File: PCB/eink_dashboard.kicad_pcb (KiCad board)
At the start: 2 copper layers, 60 parts, among them J1 USB_B_Micro, J2 Conn_01x05, Q1 IRLML6402, Q2 IRLML6402, Q3 IRLML6402, Q4 IRLML6402, U1 LM358, U10 CD4094, U11 CD4094, U2 MCP73831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

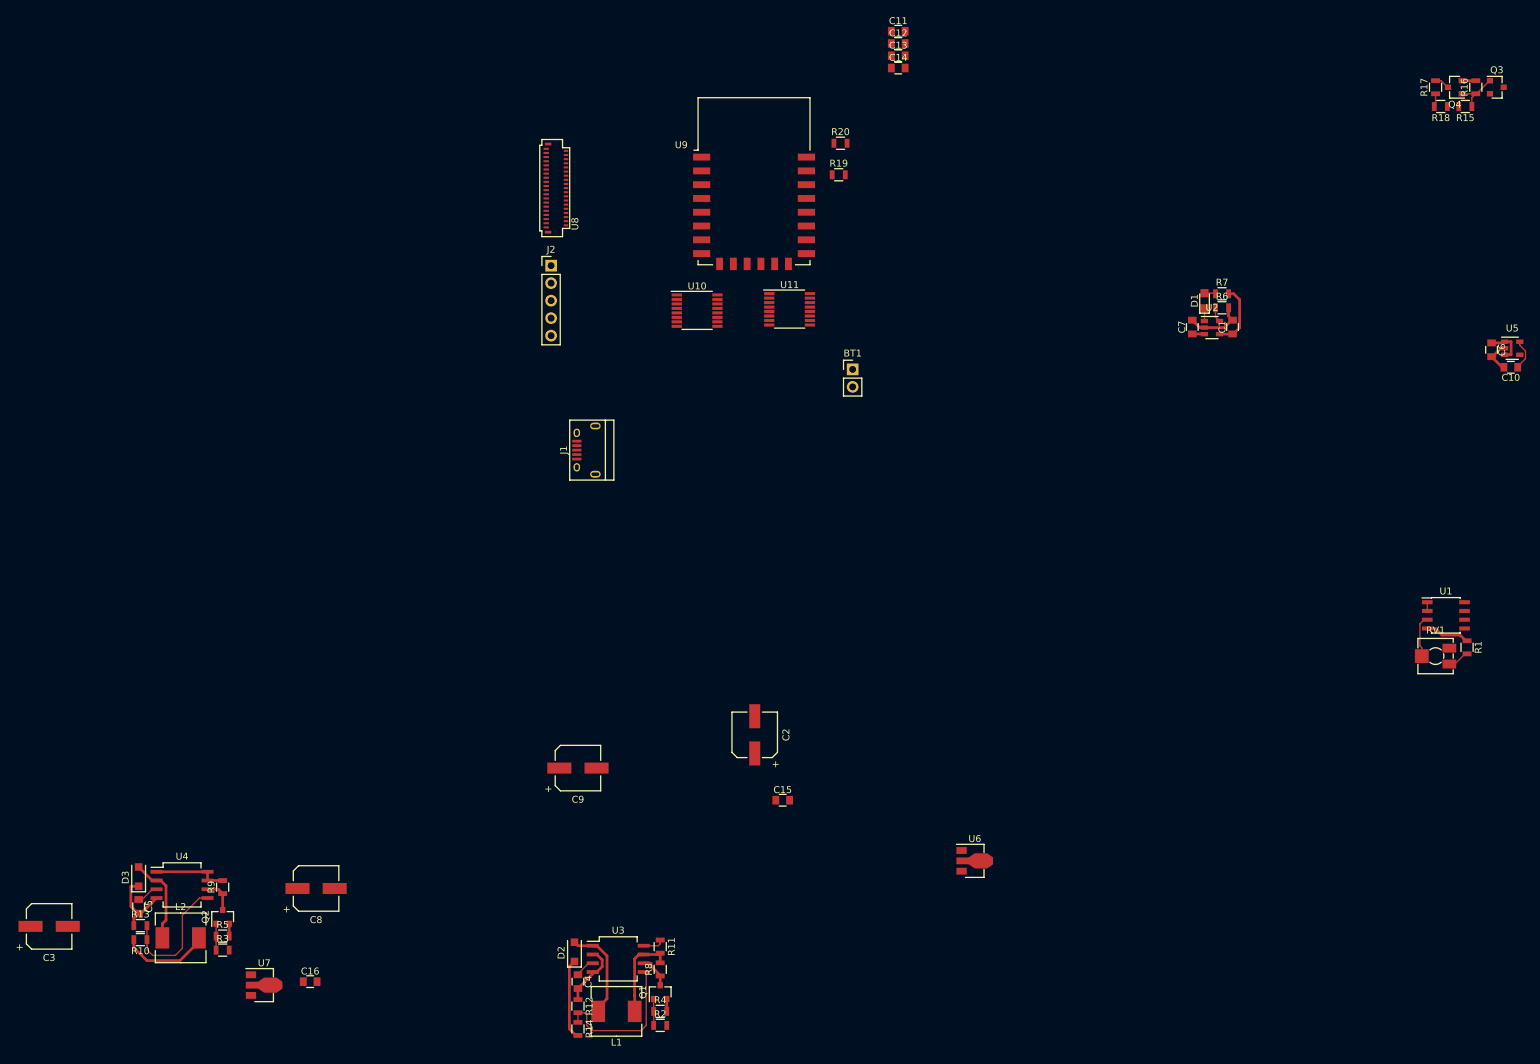
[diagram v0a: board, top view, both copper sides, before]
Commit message: PCB mostly routed
Final board layout defined
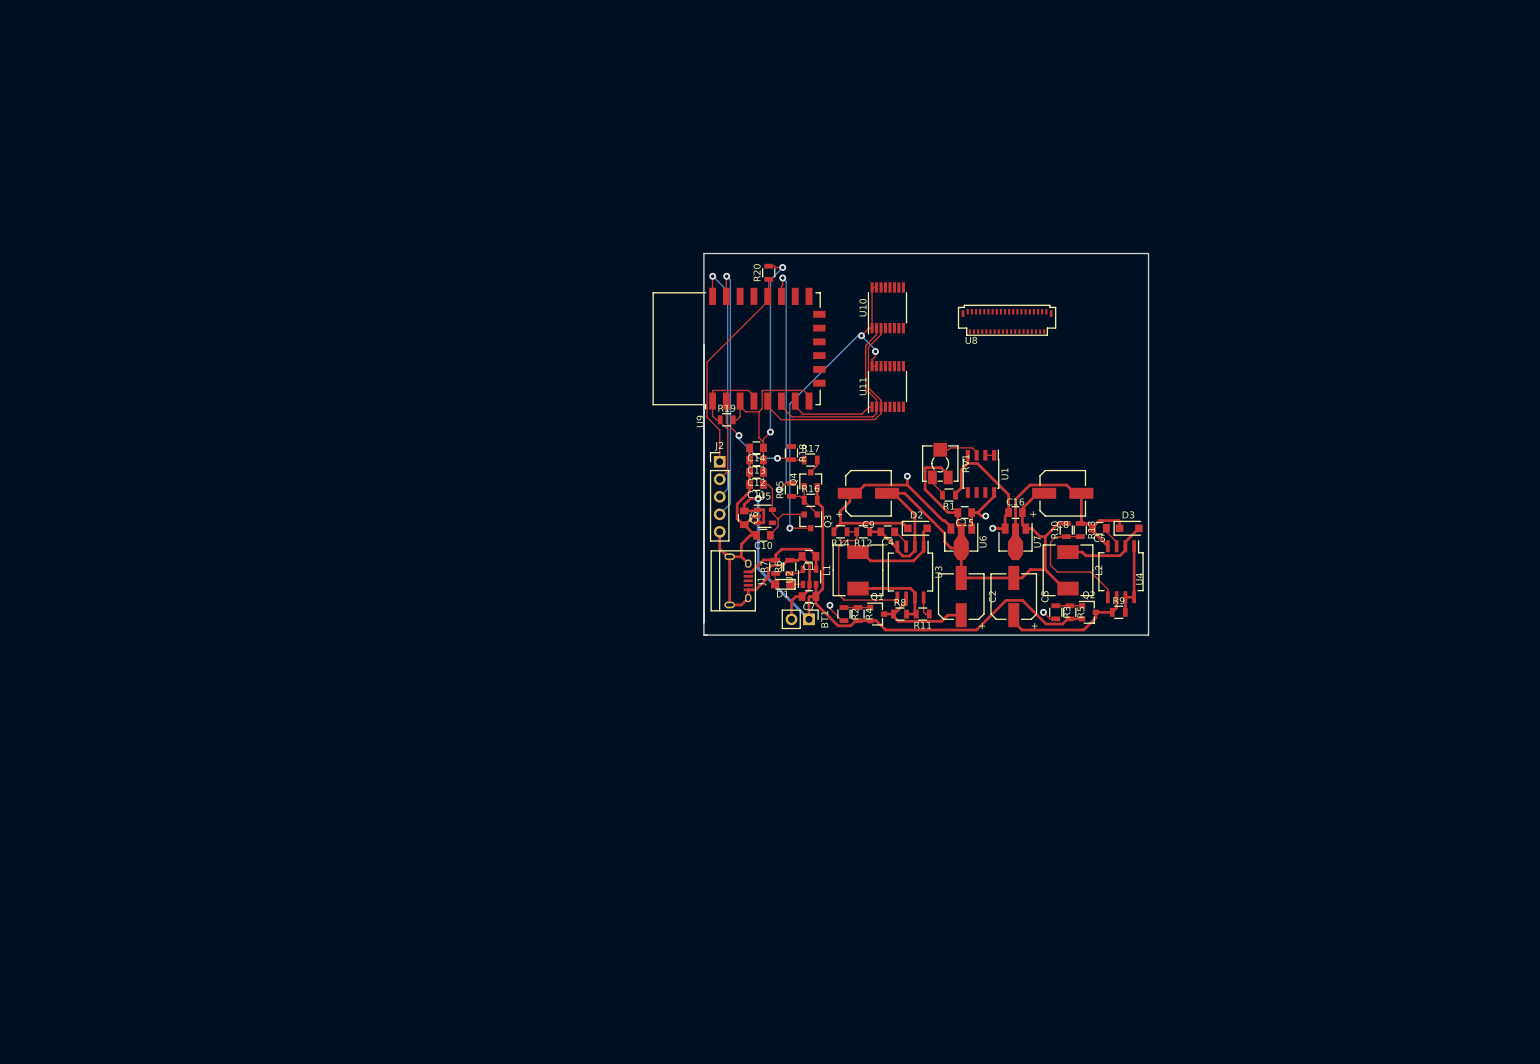
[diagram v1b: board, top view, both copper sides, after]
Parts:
- moved D3 152.4 mm to (180.8, 106.7), turned to 0 degrees
- moved C5 149.9 mm to (176.5, 106.7), turned to 180 degrees
- moved R13 148.0 mm to (173.7, 106.9), turned to 270 degrees
- moved C3 147.9 mm to (164.1, 116.6), turned to 90 degrees
- moved R10 146.9 mm to (171.7, 106.9), turned to 90 degrees
- moved U4 143.6 mm to (179.6, 113.0), turned to 270 degrees
- moved L2 139.4 mm to (172.0, 112.8), turned to 270 degrees
- moved R9 136.0 mm to (179.3, 118.9), turned to 0 degrees
- moved Q2 133.3 mm to (175.0, 118.9), turned to 0 degrees
- moved R5 131.6 mm to (172.2, 118.9), turned to 270 degrees
- moved R3 130.5 mm to (170.2, 118.9), turned to 270 degrees
- moved U7 127.2 mm to (164.3, 108.2), turned to 270 degrees
- moved C16 122.9 mm to (164.3, 104.4)
- moved C8 122.6 mm to (171.2, 101.6)
- moved Q3 117.8 mm to (134.6, 105.7), turned to 270 degrees
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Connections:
- U9 pad 6: STR -> D
- U9 pad 7: D -> STR
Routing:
- net GND: track 35.4 -> 156.4 mm
- net +BATT: track 13.1 -> 97.8 mm, vias 0 -> 1
- net +3V3: track 4.60 -> 71.1 mm, vias 0 -> 2
- net EINK_VDD: track 0.00 -> 50.2 mm, vias 0 -> 3
- net Net-(J2-Pad4): track 0.00 -> 38.3 mm, vias 0 -> 1
- net Net-(J2-Pad3): track 0.00 -> 36.3 mm, vias 0 -> 1
- net EINK_EN: track 0.00 -> 36.3 mm, vias 0 -> 2
- net CLK: track 0.00 -> 32.3 mm
- net Net-(J2-Pad1): track 0.00 -> 31.0 mm
- net D: track 0.00 -> 29.1 mm
- net -20V: track 11.1 -> 35.5 mm
- net +22V: track 11.7 -> 35.8 mm, vias 0 -> 1
- net ~RST: track 0.00 -> 21.7 mm
- net Net-(R17-Pad1): track 1.92 -> 17.0 mm, vias 0 -> 2
- net Net-(C3-Pad1): track 4.82 -> 19.7 mm
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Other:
- board outline added: 64.5 x 55.4 mm

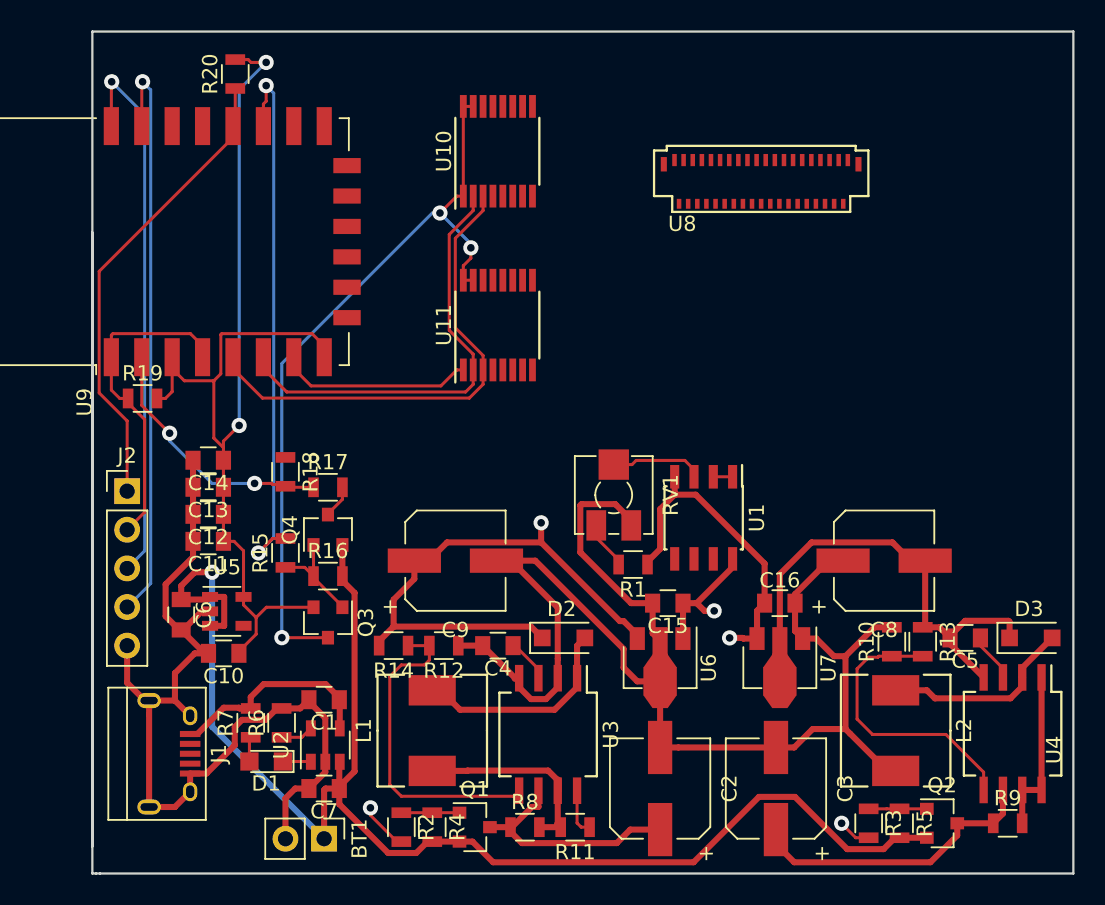
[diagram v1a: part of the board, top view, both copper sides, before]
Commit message: Finished routing board
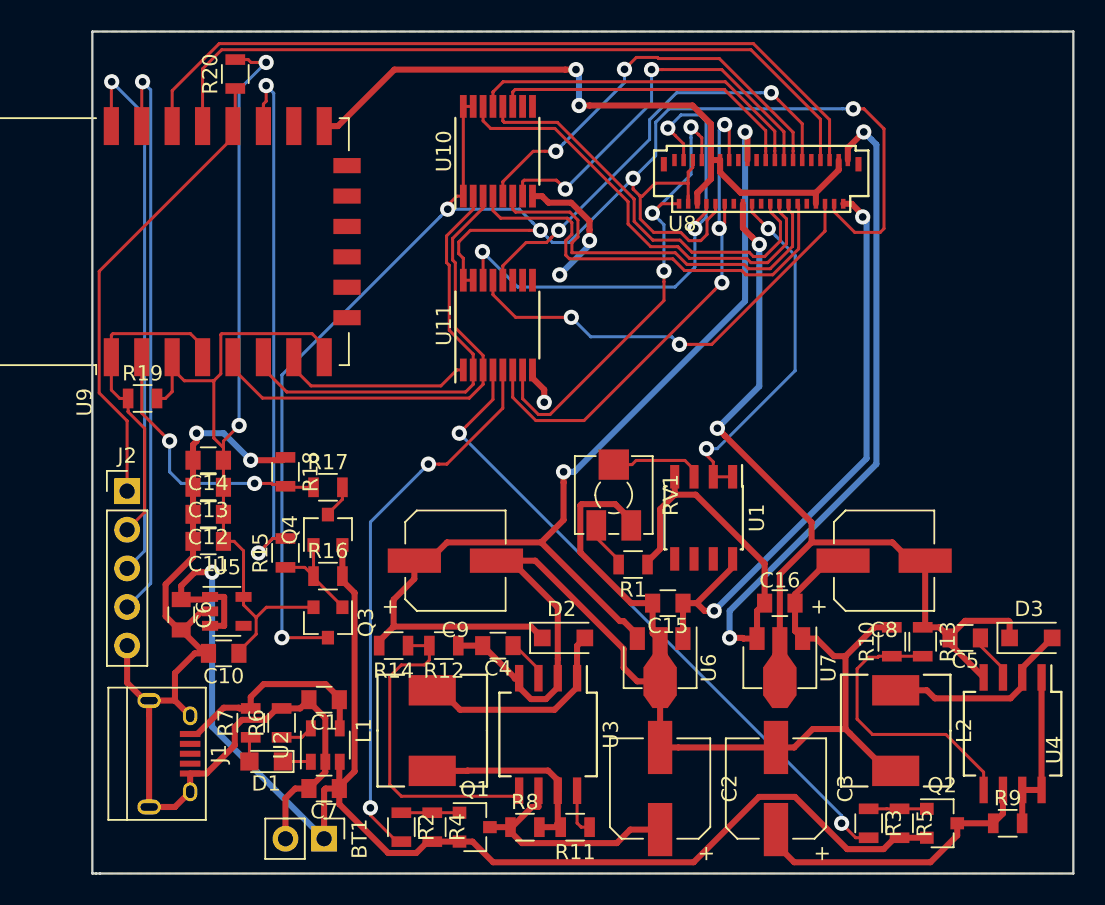
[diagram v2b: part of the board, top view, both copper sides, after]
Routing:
- net GND: track 156.4 -> 223.3 mm, vias 0 -> 7
- net EINK_VDD: track 50.2 -> 116.2 mm, vias 3 -> 5
- net CL: track 0.00 -> 51.6 mm
- net OE: track 0.00 -> 49.5 mm
- net NEG_EN: track 2.18 -> 43.3 mm, vias 1 -> 2
- net -15V: track 21.3 -> 61.2 mm, vias 1 -> 2
- net GMODE: track 0.00 -> 34.8 mm, vias 0 -> 3
- net SPV: track 0.00 -> 34.8 mm, vias 0 -> 3
- net +22V: track 35.8 -> 69.4 mm, vias 1 -> 2
- net POS_EN: track 3.24 -> 36.4 mm, vias 1 -> 2
- net CKV: track 0.00 -> 32.0 mm, vias 0 -> 3
- net +15V: track 8.48 -> 40.4 mm, vias 1 -> 2
- net SPH: track 0.00 -> 29.3 mm, vias 0 -> 2
- net LE: track 0.00 -> 29.0 mm, vias 0 -> 2
- net Net-(U10-Pad14): track 0.00 -> 29.0 mm
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- added copper zone on B.Cu, net GND
- added copper zone on F.Cu, net GND
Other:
- outline, holes or cut-outs redrawn

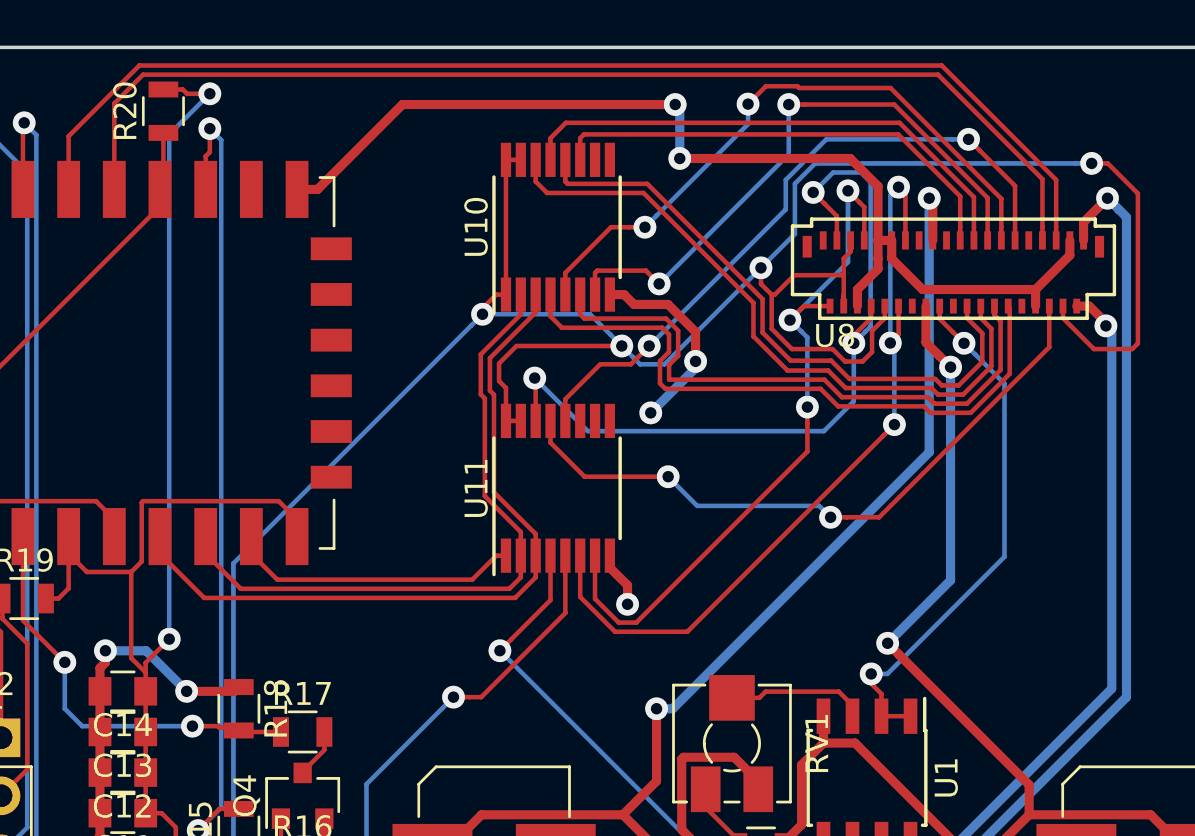
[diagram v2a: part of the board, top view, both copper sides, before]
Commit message: Shift registers moved farther apart
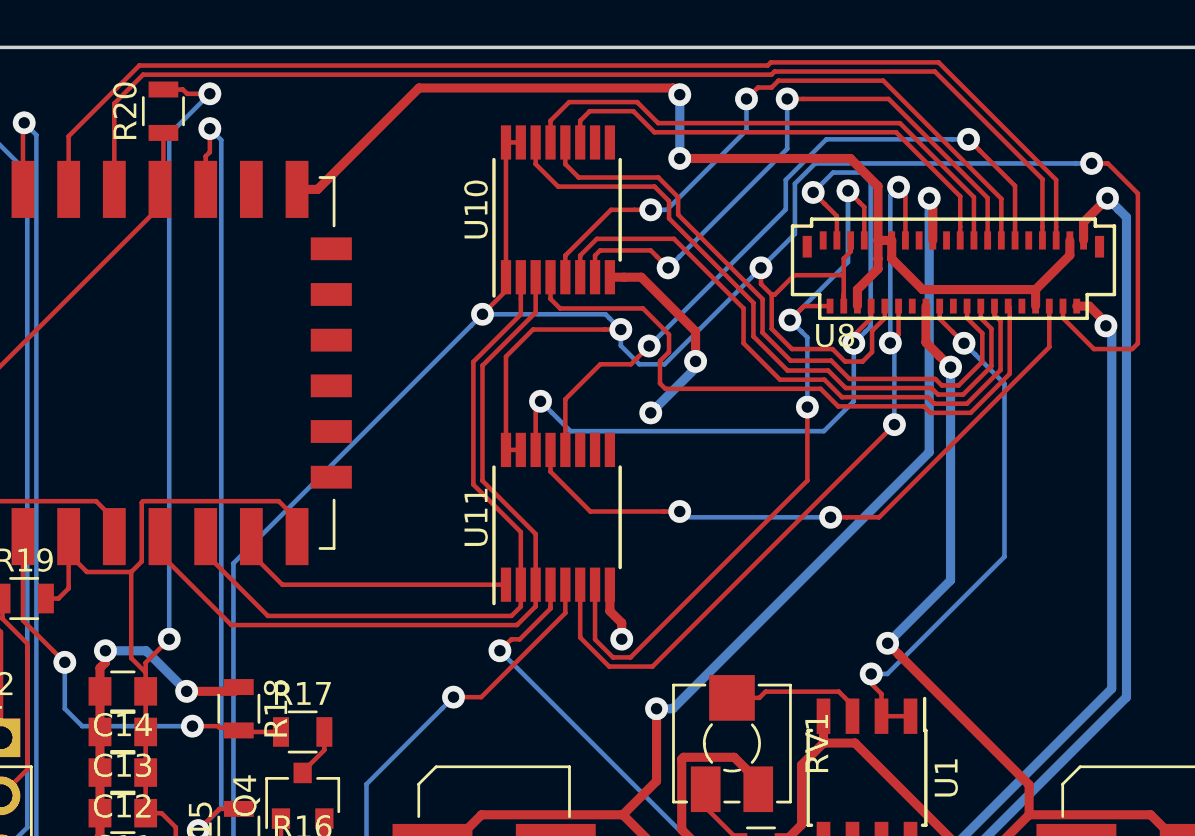
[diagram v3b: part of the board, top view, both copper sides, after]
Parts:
- moved U11 1.27 mm to (145.8, 87.4)
- moved U10 0.76 mm to (145.8, 73.9)
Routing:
- net D: track 29.2 -> 32.0 mm
- net CLK: track 32.4 -> 35.2 mm
- net EINK_VDD: track 116.2 -> 118.7 mm
- net CKV: track 32.0 -> 33.8 mm
- net GND: track 223.3 -> 224.7 mm
- net SPH: track 29.3 -> 30.6 mm
- net POS_EN: track 36.4 -> 35.1 mm
- net NEG_EN: track 43.3 -> 42.3 mm
- net GMODE: track 34.8 -> 35.8 mm
- net Net-(U10-Pad6): track 26.2 -> 27.1 mm
- net Net-(U10-Pad14): track 29.0 -> 29.7 mm
- net Net-(U10-Pad12): track 26.9 -> 27.7 mm
- net LE: track 29.0 -> 28.5 mm
- net Net-(U10-Pad11): track 20.7 -> 21.2 mm

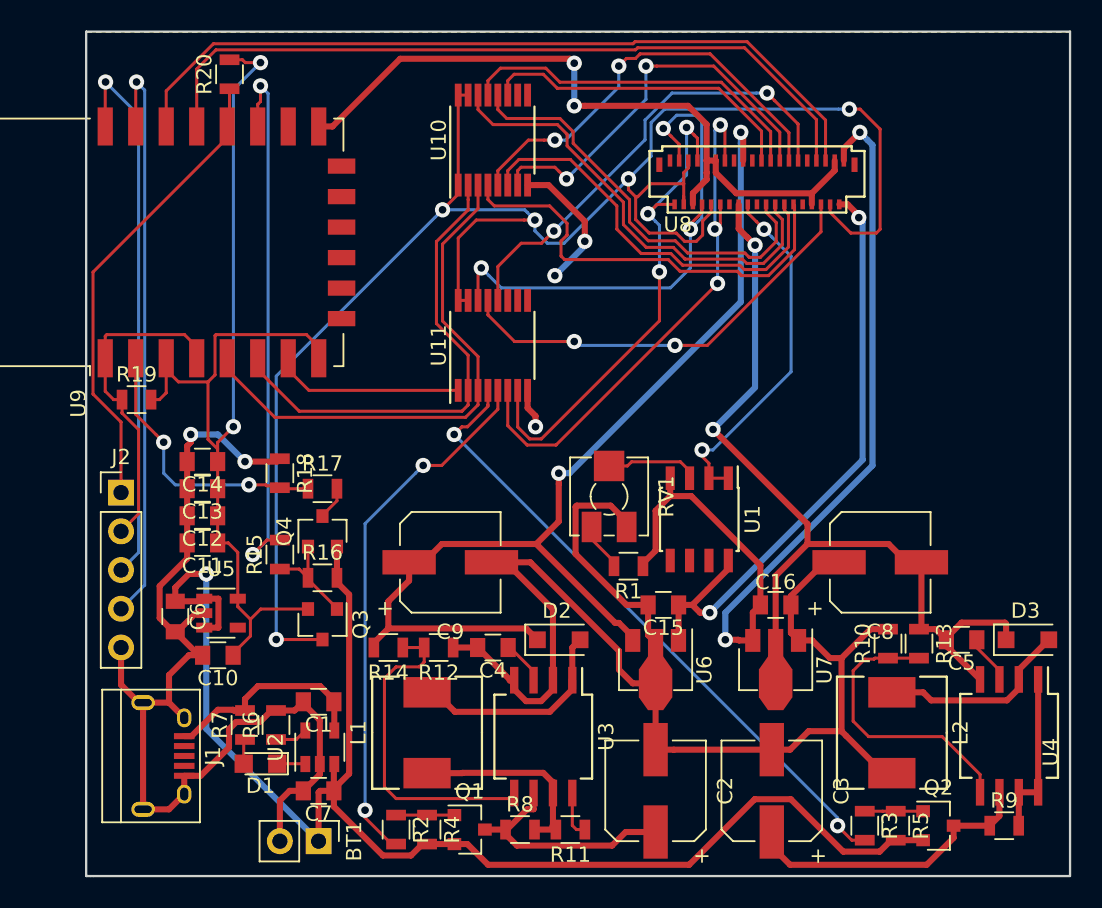
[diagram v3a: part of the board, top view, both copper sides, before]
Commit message: Tight clearances cleaned up
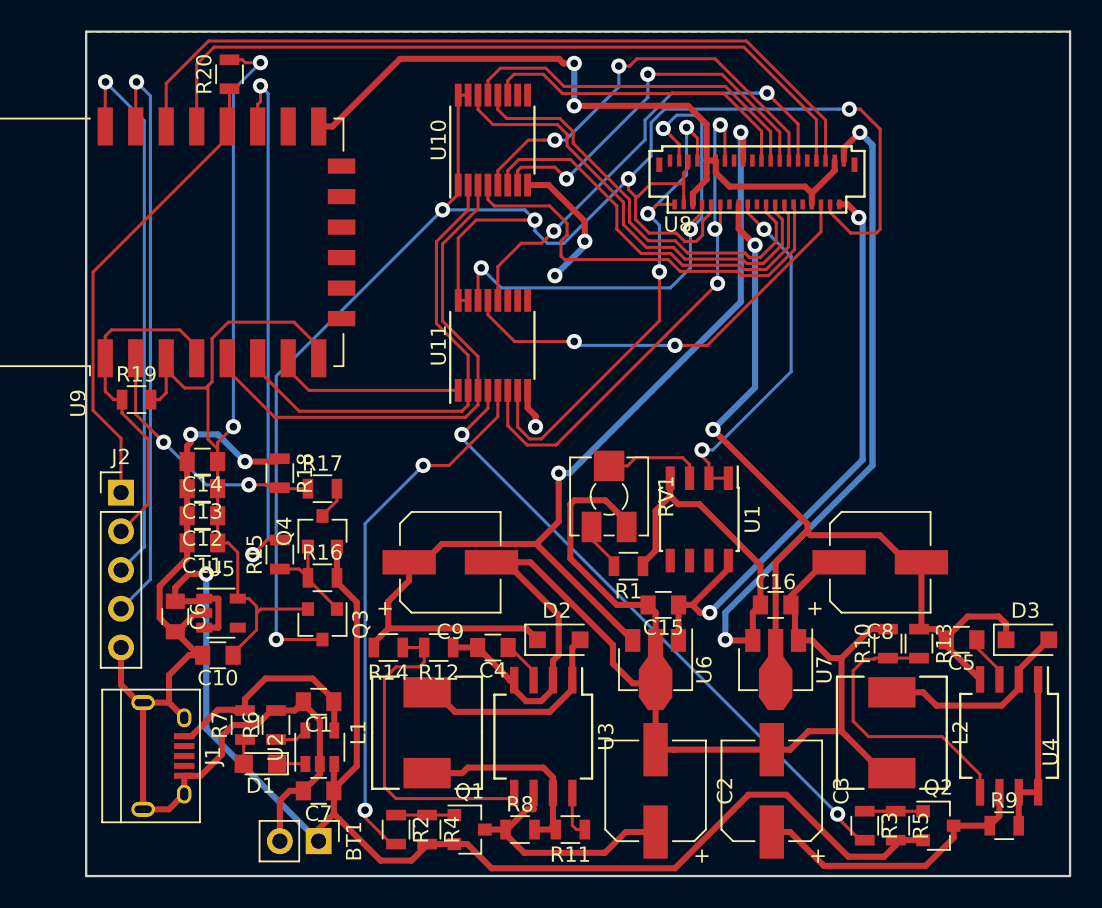
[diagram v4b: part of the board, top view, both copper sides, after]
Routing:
- net GND: track 224.7 -> 226.3 mm
- net Net-(R17-Pad1): track 18.2 -> 17.0 mm
- net +3V3: track 71.1 -> 72.2 mm
- net NEG_EN: track 42.3 -> 41.3 mm
- net Net-(U10-Pad7): track 26.5 -> 25.7 mm
- net ~RST: track 21.7 -> 22.4 mm
- net -20V: track 61.9 -> 62.6 mm
- net Net-(C3-Pad1): track 19.7 -> 19.2 mm
